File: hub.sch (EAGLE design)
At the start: 26 parts, among them U1 10118194-MICRO-USB, U2 LM3671MF-3.3/NOPBMF05A-M, U3 SN74LVC1T45DBVRDBV6-M, U4 SN74LVC1T45DBVRDBV6-M

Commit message: More component arrangement
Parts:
- JP7: value (none) -> GPIO
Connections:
- net GND: now also U1.GND$1, U1.GND$2, U1.GND$3, U1.GND$4, U1.GND$5; no longer U1.GND
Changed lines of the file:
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@@
 <part name="GND18" library="supply1" library_urn="urn:adsk.eagle:library:371" deviceset="GND" device=""/>
 <part name="U$2" library="nebrius" deviceset="ESP32-WROOM-32D" device=""/>
-<part name="JP7" library="pinhead" library_urn="urn:adsk.eagle:library:325" deviceset="PINHD-2X5" device="" package3d_urn="urn:adsk.eagle:package:22470/2"/>
+<part name="JP7" library="pinhead" library_urn="urn:adsk.eagle:library:325" deviceset="PINHD-2X5" device="" package3d_urn="urn:adsk.eagle:package:22470/2" value="GPIO"/>
 <part name="GND23" library="supply1" library_urn="urn:adsk.eagle:library:371" deviceset="GND" device=""/>
 <part name="P+10" library="supply1" library_urn="urn:adsk.eagle:library:371" deviceset="VCC" device=""/>
@@
 <part name="GND17" library="supply1" library_urn="urn:adsk.eagle:library:371" deviceset="GND" device=""/>
 <part name="P+9" library="supply1" library_urn="urn:adsk.eagle:library:371" deviceset="VCC" device=""/>
+<part name="GND20" library="supply1" library_urn="urn:adsk.eagle:library:371" deviceset="GND" device=""/>
 </parts>
 <sheets>
@@
 <attribute name="VALUE" x="139.7" y="0" size="1.778" layer="96"/>
 </instance>
+<instance part="GND20" gate="1" x="5.08" y="12.7" smashed="yes">
+<attribute name="VALUE" x="2.54" y="10.16" size="1.778" layer="96"/>
+</instance>
 </instances>
 <busses>
@@
 <net name="GND" class="0">
 <segment>
-<pinref part="U1" gate="G$1" pin="GND"/>
+<pinref part="U1" gate="G$1" pin="GND$1"/>
 <pinref part="GND1" gate="1" pin="GND"/>
 <wire x1="38.1" y1="17.78" x2="40.64" y2="17.78" width="0.1524" layer="91"/>
@@
 <wire x1="142.24" y1="5.08" x2="142.24" y2="7.62" width="0.1524" layer="91"/>
 </segment>
+<segment>
+<pinref part="U1" gate="G$1" pin="GND$2"/>
+<pinref part="GND20" gate="1" pin="GND"/>
+<wire x1="7.62" y1="25.4" x2="5.08" y2="25.4" width="0.1524" layer="91"/>
+<wire x1="5.08" y1="25.4" x2="5.08" y2="22.86" width="0.1524" layer="91"/>
+<pinref part="U1" gate="G$1" pin="GND$3"/>
+<wire x1="5.08" y1="22.86" x2="5.08" y2="20.32" width="0.1524" layer="91"/>
+<wire x1="5.08" y1="20.32" x2="5.08" y2="17.78" width="0.1524" layer="91"/>
+<wire x1="5.08" y1="17.78" x2="5.08" y2="15.24" width="0.1524" layer="91"/>
+<wire x1="7.62" y1="22.86" x2="5.08" y2="22.86" width="0.1524" layer="91"/>
+<junction x="5.08" y="22.86"/>
+<pinref part="U1" gate="G$1" pin="GND$4"/>
+<wire x1="7.62" y1="20.32" x2="5.08" y2="20.32" width="0.1524" layer="91"/>
+<junction x="5.08" y="20.32"/>
+<pinref part="U1" gate="G$1" pin="GND$5"/>
+<wire x1="7.62" y1="17.78" x2="5.08" y2="17.78" width="0.1524" layer="91"/>
+<junction x="5.08" y="17.78"/>
+</segment>
 </net>

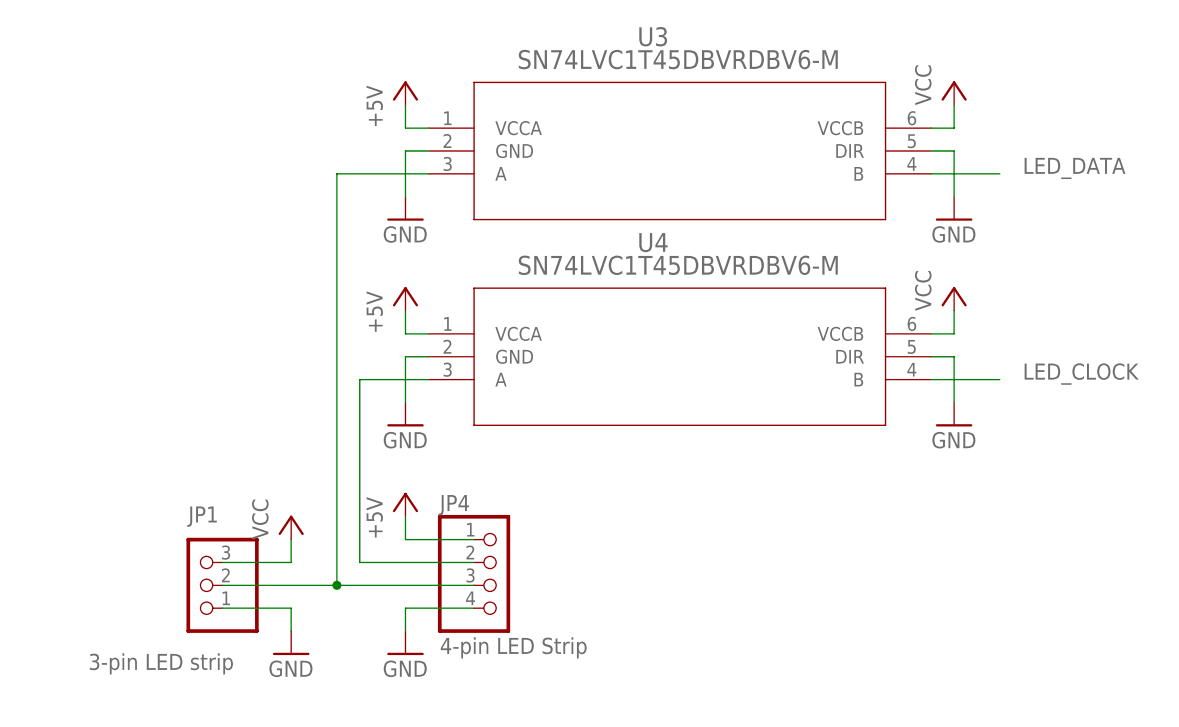
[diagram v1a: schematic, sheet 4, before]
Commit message: First draft of device placement
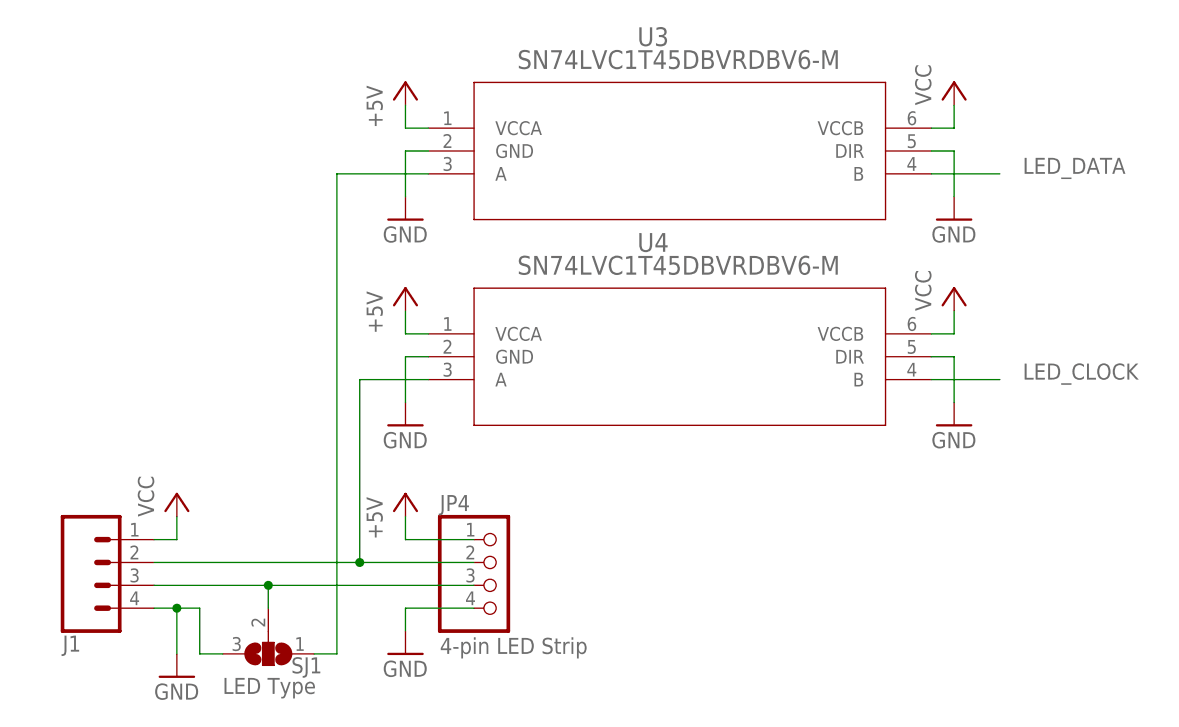
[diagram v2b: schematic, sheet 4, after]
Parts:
- removed JP1: 3-pin LED strip, pinhead:PINHD-1X3/90
- added J1: (no value), SparkFun-Connectors:CONN_04SCREW
- added SJ1: LED Type, jumper:SJ2W
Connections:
- new net N$7: J1.3, JP4.3, SJ1.2
- net GND: now also J1.4, SJ1.3; no longer JP1.1
- net N$8: now also SJ1.1; no longer JP1.2, JP4.3
- net N$9: now also J1.2
- net VCC: now also J1.1, JP2.3; no longer JP1.3
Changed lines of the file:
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@@
 <layer number="112" name="tSilk" color="7" fill="1" visible="no" active="yes"/>
 <layer number="113" name="IDFDebug" color="4" fill="1" visible="no" active="yes"/>
+<layer number="114" name="Badge_Outline" color="7" fill="1" visible="yes" active="yes"/>
+<layer number="115" name="ReferenceISLANDS" color="7" fill="1" visible="yes" active="yes"/>
 <layer number="116" name="Patch_BOT" color="9" fill="4" visible="no" active="yes"/>
 <layer number="118" name="Rect_Pads" color="7" fill="1" visible="no" active="yes"/>
@@
 <layer number="230" name="230bmp" color="7" fill="1" visible="no" active="yes"/>
 <layer number="231" name="231bmp" color="7" fill="1" visible="no" active="yes"/>
+<layer number="232" name="Eagle3D_PG2" color="7" fill="1" visible="yes" active="yes"/>
+<layer number="233" name="Eagle3D_PG3" color="7" fill="1" visible="yes" active="yes"/>
 <layer number="248" name="Housing" color="7" fill="1" visible="no" active="yes"/>
 <layer number="249" name="Edge" color="7" fill="1" visible="no" active="yes"/>
@@
 <part name="JP3" library="pinhead" library_urn="urn:adsk.eagle:library:325" deviceset="PINHD-2X3" device="" package3d_urn="urn:adsk.eagle:package:22462/2" value="JTAG"/>
 <part name="GND16" library="supply1" library_urn="urn:adsk.eagle:library:371" deviceset="GND" device=""/>
-<part name="JP1" library="pinhead" library_urn="urn:adsk.eagle:library:325" deviceset="PINHD-1X3" device="/90" package3d_urn="urn:adsk.eagle:package:22459/2" value="3-pin LED strip"/>
+<part name="GND20" library="supply1" library_urn="urn:adsk.eagle:library:371" deviceset="GND" device=""/>
+<part name="P+14" library="supply1" library_urn="urn:adsk.eagle:library:371" deviceset="VCC" device=""/>
+<part name="J1" library="SparkFun-Connectors" library_urn="urn:adsk.eagle:library:513" deviceset="CONN_04" device="SCREW" package3d_urn="urn:adsk.eagle:package:38090/1"/>
+<part name="P+9" library="supply1" library_urn="urn:adsk.eagle:library:371" deviceset="VCC" device=""/>
 <part name="GND17" library="supply1" library_urn="urn:adsk.eagle:library:371" deviceset="GND" device=""/>
-<part name="P+9" library="supply1" library_urn="urn:adsk.eagle:library:371" deviceset="VCC" device=""/>
-<part name="GND20" library="supply1" library_urn="urn:adsk.eagle:library:371" deviceset="GND" device=""/>
+<part name="SJ1" library="jumper" library_urn="urn:adsk.eagle:library:252" deviceset="SJ2W" device="" package3d_urn="urn:adsk.eagle:package:15474/1" value="LED Type"/>
 </parts>
 <sheets>
@@
 <attribute name="VALUE" x="25.4" y="43.18" size="1.778" layer="96" rot="R180"/>
 </instance>
+<instance part="P+14" gate="VCC" x="68.58" y="60.96" smashed="yes">
+<attribute name="VALUE" x="66.04" y="58.42" size="1.778" layer="96" rot="R90"/>
+</instance>
 </instances>
 <busses>
@@
 </segment>
 </net>
+<net name="VCC" class="0">
+<segment>
+<pinref part="JP2" gate="A" pin="3"/>
+<pinref part="P+14" gate="VCC" pin="VCC"/>
+<wire x1="78.74" y1="50.8" x2="68.58" y2="50.8" width="0.1524" layer="91"/>
+<wire x1="68.58" y1="50.8" x2="68.58" y2="58.42" width="0.1524" layer="91"/>
+</segment>
+</net>
 </nets>
 </sheet>
@@
 <attribute name="VALUE" x="19.05" y="43.18" size="1.778" layer="96"/>
 </instance>
-<instance part="JP1" gate="A" x="-7.62" y="50.8" smashed="yes" rot="R180">
-<attribute name="NAME" x="-8.89" y="57.785" size="1.778" layer="95" rot="R180" align="top-right"/>
-<attribute name="VALUE" x="-3.81" y="43.18" size="1.778" layer="96" rot="R180"/>
-</instance>
-<instance part="GND17" gate="1" x="2.54" y="43.18" smashed="yes">
-<attribute name="VALUE" x="0" y="40.64" size="1.778" layer="96"/>
-</instance>
-<instance part="P+9" gate="VCC" x="2.54" y="58.42" smashed="yes">
-<attribute name="VALUE" x="0" y="55.88" size="1.778" layer="96" rot="R90"/>
+<instance part="J1" gate="G$1" x="-17.78" y="53.34" smashed="yes" rot="MR180">
+<attribute name="VALUE" x="-22.86" y="60.706" size="1.778" layer="96" font="vector" rot="MR180"/>
+<attribute name="NAME" x="-22.86" y="45.212" size="1.778" layer="95" font="vector" rot="MR180"/>
+</instance>
+<instance part="P+9" gate="VCC" x="-10.16" y="60.96" smashed="yes">
+<attribute name="VALUE" x="-12.7" y="58.42" size="1.778" layer="96" rot="R90"/>
+</instance>
+<instance part="GND17" gate="1" x="-10.16" y="40.64" smashed="yes">
+<attribute name="VALUE" x="-12.7" y="38.1" size="1.778" layer="96"/>
+</instance>
+<instance part="SJ1" gate="G$1" x="0" y="43.18" smashed="yes" rot="R270">
+<attribute name="NAME" x="2.54" y="41.021" size="1.778" layer="95"/>
+<attribute name="VALUE" x="-5.08" y="38.735" size="1.778" layer="96"/>
 </instance>
 </instances>
@@
 </segment>
 <segment>
-<pinref part="JP1" gate="A" pin="1"/>
 <pinref part="GND17" gate="1" pin="GND"/>
-<wire x1="-5.08" y1="48.26" x2="2.54" y2="48.26" width="0.1524" layer="91"/>
-<wire x1="2.54" y1="48.26" x2="2.54" y2="45.72" width="0.1524" layer="91"/>
+<wire x1="-10.16" y1="48.26" x2="-10.16" y2="43.18" width="0.1524" layer="91"/>
+<pinref part="J1" gate="G$1" pin="4"/>
+<wire x1="-12.7" y1="48.26" x2="-10.16" y2="48.26" width="0.1524" layer="91"/>
+<wire x1="-5.08" y1="43.18" x2="-7.62" y2="43.18" width="0.1524" layer="91"/>
+<wire x1="-7.62" y1="43.18" x2="-7.62" y2="48.26" width="0.1524" layer="91"/>
+<wire x1="-7.62" y1="48.26" x2="-10.16" y2="48.26" width="0.1524" layer="91"/>
+<junction x="-10.16" y="48.26"/>
+<pinref part="SJ1" gate="G$1" pin="3"/>
 </segment>
 </net>
@@
 </segment>
 <segment>
-<pinref part="JP1" gate="A" pin="3"/>
-<wire x1="-5.08" y1="53.34" x2="2.54" y2="53.34" width="0.1524" layer="91"/>
 <pinref part="P+9" gate="VCC" pin="VCC"/>
-<wire x1="2.54" y1="53.34" x2="2.54" y2="55.88" width="0.1524" layer="91"/>
+<wire x1="-10.16" y1="55.88" x2="-10.16" y2="58.42" width="0.1524" layer="91"/>
+<pinref part="J1" gate="G$1" pin="1"/>
+<wire x1="-12.7" y1="55.88" x2="-10.16" y2="55.88" width="0.1524" layer="91"/>
 </segment>
 </net>
@@
 <segment>
 <pinref part="U3" gate="A" pin="A"/>
-<wire x1="7.62" y1="50.8" x2="7.62" y2="96.52" width="0.1524" layer="91"/>
 <wire x1="7.62" y1="96.52" x2="17.78" y2="96.52" width="0.1524" layer="91"/>
-<pinref part="JP1" gate="A" pin="2"/>
-<wire x1="-5.08" y1="50.8" x2="7.62" y2="50.8" width="0.1524" layer="91"/>
-<pinref part="JP4" gate="A" pin="3"/>
-<wire x1="22.86" y1="50.8" x2="7.62" y2="50.8" width="0.1524" layer="91"/>
-<junction x="7.62" y="50.8"/>
+<wire x1="7.62" y1="96.52" x2="7.62" y2="43.18" width="0.1524" layer="91"/>
+<wire x1="7.62" y1="43.18" x2="5.08" y2="43.18" width="0.1524" layer="91"/>
+<pinref part="SJ1" gate="G$1" pin="1"/>
 </segment>
 </net>
@@
 <wire x1="22.86" y1="53.34" x2="10.16" y2="53.34" width="0.1524" layer="91"/>
 <wire x1="10.16" y1="53.34" x2="10.16" y2="73.66" width="0.1524" layer="91"/>
+<pinref part="J1" gate="G$1" pin="2"/>
+<wire x1="-12.7" y1="53.34" x2="10.16" y2="53.34" width="0.1524" layer="91"/>
+<junction x="10.16" y="53.34"/>
 </segment>
 </net>
@@
 </segment>
 </net>
+<net name="N$7" class="0">
+<segment>
+<wire x1="0" y1="48.26" x2="0" y2="50.8" width="0.1524" layer="91"/>
+<pinref part="JP4" gate="A" pin="3"/>
+<wire x1="0" y1="50.8" x2="22.86" y2="50.8" width="0.1524" layer="91"/>
+<pinref part="J1" gate="G$1" pin="3"/>
+<wire x1="-12.7" y1="50.8" x2="0" y2="50.8" width="0.1524" layer="91"/>
+<junction x="0" y="50.8"/>
+<pinref part="SJ1" gate="G$1" pin="2"/>
+</segment>
+</net>

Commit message: First draft of component layout
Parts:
- removed JP4: 4-pin LED Strip, pinhead:PINHD-1X4/90
- added JP1: (no value), pinhead:PINHD-1X4
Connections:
- net +5V: now also J1.1, JP1.1; no longer JP4.1
- net GND: now also JP1.4; no longer JP4.4
- net N$7: now also JP1.3; no longer JP4.3
- net N$9: now also JP1.2; no longer JP4.2
- net VCC: no longer J1.1
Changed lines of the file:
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@@
 <part name="R4" library="rcl" library_urn="urn:adsk.eagle:library:334" deviceset="R-US_" device="R0805" package3d_urn="urn:adsk.eagle:package:23553/2" value="10k"/>
 <part name="P+12" library="supply1" library_urn="urn:adsk.eagle:library:371" deviceset="VCC" device=""/>
-<part name="JP4" library="pinhead" library_urn="urn:adsk.eagle:library:325" deviceset="PINHD-1X4" device="/90" package3d_urn="urn:adsk.eagle:package:22404/2" value="4-pin LED Strip"/>
 <part name="R6" library="rcl" library_urn="urn:adsk.eagle:library:334" deviceset="R-US_" device="R0805" package3d_urn="urn:adsk.eagle:package:23553/2" value="220"/>
 <part name="LED1" library="led" library_urn="urn:adsk.eagle:library:259" deviceset="LED" device="CHIPLED_0805" package3d_urn="urn:adsk.eagle:package:15821/2" value="Power"/>
@@
 <part name="P+14" library="supply1" library_urn="urn:adsk.eagle:library:371" deviceset="VCC" device=""/>
 <part name="J1" library="SparkFun-Connectors" library_urn="urn:adsk.eagle:library:513" deviceset="CONN_04" device="SCREW" package3d_urn="urn:adsk.eagle:package:38090/1"/>
-<part name="P+9" library="supply1" library_urn="urn:adsk.eagle:library:371" deviceset="VCC" device=""/>
 <part name="GND17" library="supply1" library_urn="urn:adsk.eagle:library:371" deviceset="GND" device=""/>
 <part name="SJ1" library="jumper" library_urn="urn:adsk.eagle:library:252" deviceset="SJ2W" device="" package3d_urn="urn:adsk.eagle:package:15474/1" value="LED Type"/>
+<part name="JP1" library="pinhead" library_urn="urn:adsk.eagle:library:325" deviceset="PINHD-1X4" device="" package3d_urn="urn:adsk.eagle:package:22407/2"/>
+<part name="P+9" library="supply1" library_urn="urn:adsk.eagle:library:371" deviceset="+5V" device=""/>
 </parts>
 <sheets>
@@
 <attribute name="VALUE" x="12.7" y="55.88" size="1.778" layer="96" rot="R90"/>
 </instance>
-<instance part="JP4" gate="A" x="25.4" y="50.8" smashed="yes">
-<attribute name="NAME" x="19.05" y="59.055" size="1.778" layer="95"/>
-<attribute name="VALUE" x="19.05" y="43.18" size="1.778" layer="96"/>
-</instance>
 <instance part="J1" gate="G$1" x="-17.78" y="53.34" smashed="yes" rot="MR180">
 <attribute name="VALUE" x="-22.86" y="60.706" size="1.778" layer="96" font="vector" rot="MR180"/>
 <attribute name="NAME" x="-22.86" y="45.212" size="1.778" layer="95" font="vector" rot="MR180"/>
 </instance>
-<instance part="P+9" gate="VCC" x="-10.16" y="60.96" smashed="yes">
-<attribute name="VALUE" x="-12.7" y="58.42" size="1.778" layer="96" rot="R90"/>
-</instance>
 <instance part="GND17" gate="1" x="-10.16" y="40.64" smashed="yes">
 <attribute name="VALUE" x="-12.7" y="38.1" size="1.778" layer="96"/>
@@
 <attribute name="NAME" x="2.54" y="41.021" size="1.778" layer="95"/>
 <attribute name="VALUE" x="-5.08" y="38.735" size="1.778" layer="96"/>
+</instance>
+<instance part="JP1" gate="A" x="25.4" y="50.8" smashed="yes">
+<attribute name="NAME" x="19.05" y="59.055" size="1.778" layer="95"/>
+<attribute name="VALUE" x="19.05" y="43.18" size="1.778" layer="96"/>
+</instance>
+<instance part="P+9" gate="1" x="-10.16" y="60.96" smashed="yes">
+<attribute name="VALUE" x="-5.08" y="55.88" size="1.778" layer="96" rot="R90"/>
 </instance>
 </instances>
@@
 <wire x1="22.86" y1="48.26" x2="15.24" y2="48.26" width="0.1524" layer="91"/>
 <wire x1="15.24" y1="48.26" x2="15.24" y2="45.72" width="0.1524" layer="91"/>
-<pinref part="JP4" gate="A" pin="4"/>
+<pinref part="JP1" gate="A" pin="4"/>
 </segment>
 <segment>
@@
 <wire x1="76.2" y1="78.74" x2="76.2" y2="81.28" width="0.1524" layer="91"/>
 </segment>
-<segment>
-<pinref part="P+9" gate="VCC" pin="VCC"/>
-<wire x1="-10.16" y1="55.88" x2="-10.16" y2="58.42" width="0.1524" layer="91"/>
-<pinref part="J1" gate="G$1" pin="1"/>
-<wire x1="-12.7" y1="55.88" x2="-10.16" y2="55.88" width="0.1524" layer="91"/>
-</segment>
 </net>
 <net name="N$8" class="0">
@@
 <pinref part="U4" gate="A" pin="A"/>
 <wire x1="10.16" y1="73.66" x2="17.78" y2="73.66" width="0.1524" layer="91"/>
-<pinref part="JP4" gate="A" pin="2"/>
 <wire x1="22.86" y1="53.34" x2="10.16" y2="53.34" width="0.1524" layer="91"/>
 <wire x1="10.16" y1="53.34" x2="10.16" y2="73.66" width="0.1524" layer="91"/>
@@
 <wire x1="-12.7" y1="53.34" x2="10.16" y2="53.34" width="0.1524" layer="91"/>
 <junction x="10.16" y="53.34"/>
+<pinref part="JP1" gate="A" pin="2"/>
 </segment>
 </net>
@@
 <wire x1="15.24" y1="55.88" x2="15.24" y2="58.42" width="0.1524" layer="91"/>
 <pinref part="P+2" gate="1" pin="+5V"/>
-<pinref part="JP4" gate="A" pin="1"/>
+<pinref part="JP1" gate="A" pin="1"/>
+</segment>
+<segment>
+<wire x1="-10.16" y1="55.88" x2="-10.16" y2="58.42" width="0.1524" layer="91"/>
+<pinref part="J1" gate="G$1" pin="1"/>
+<wire x1="-12.7" y1="55.88" x2="-10.16" y2="55.88" width="0.1524" layer="91"/>
+<pinref part="P+9" gate="1" pin="+5V"/>
 </segment>
 </net>
@@
 <segment>
 <wire x1="0" y1="48.26" x2="0" y2="50.8" width="0.1524" layer="91"/>
-<pinref part="JP4" gate="A" pin="3"/>
 <wire x1="0" y1="50.8" x2="22.86" y2="50.8" width="0.1524" layer="91"/>
 <pinref part="J1" gate="G$1" pin="3"/>
@@
 <junction x="0" y="50.8"/>
 <pinref part="SJ1" gate="G$1" pin="2"/>
-</segment>
-</net>
+<pinref part="JP1" gate="A" pin="3"/>
+</segment>
+</net>

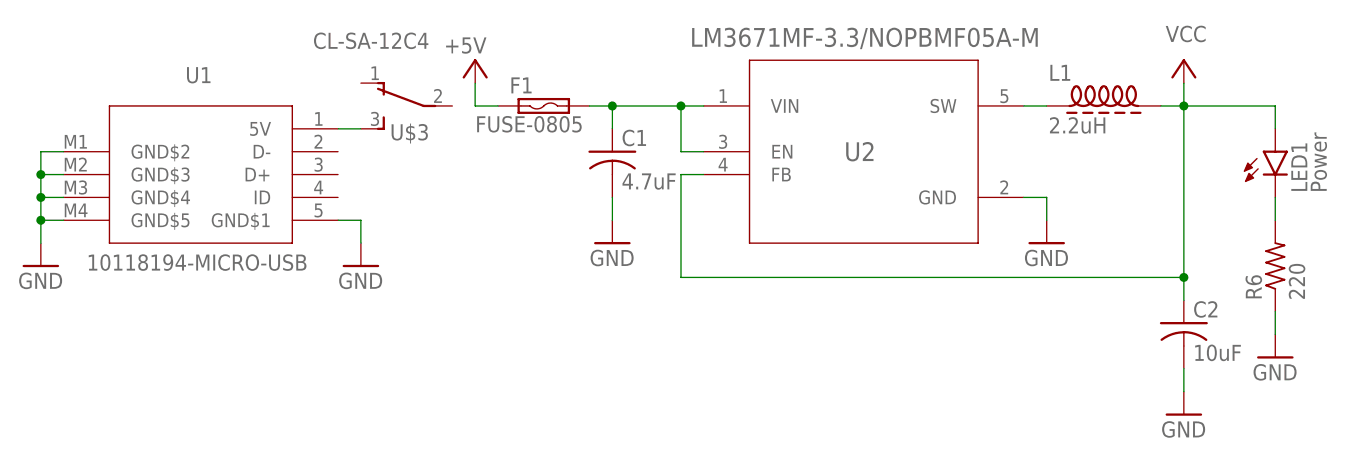
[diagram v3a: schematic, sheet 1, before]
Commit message: Finished placing components and started laying out traces
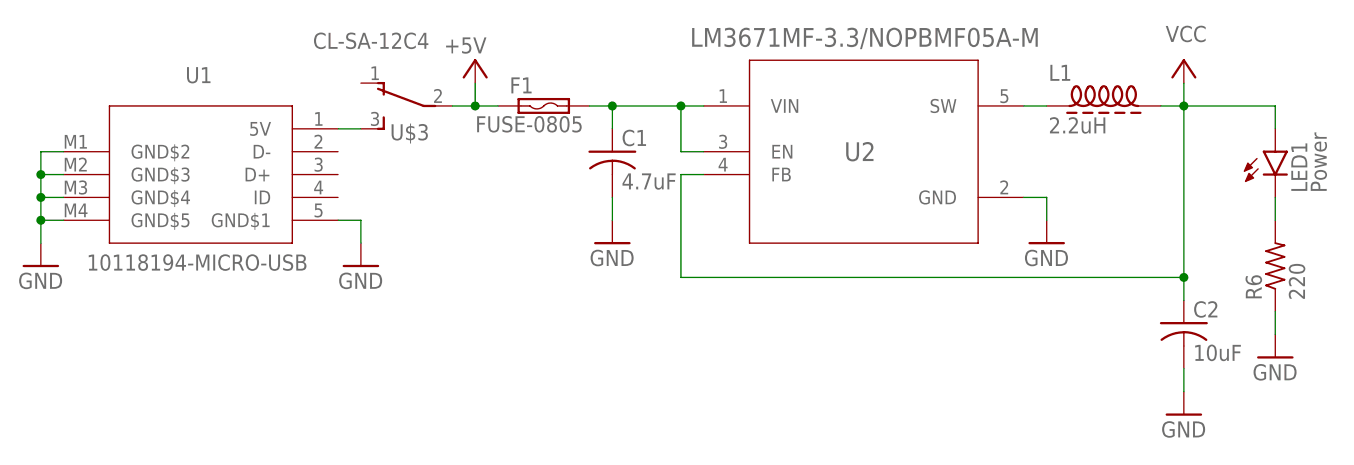
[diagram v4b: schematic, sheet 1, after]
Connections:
- net +5V: now also U$3.2
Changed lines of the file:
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@@
 <pinref part="F1" gate="A" pin="1"/>
 <pinref part="P+1" gate="1" pin="+5V"/>
+<pinref part="U$3" gate="A" pin="2"/>
+<wire x1="50.8" y1="30.48" x2="53.34" y2="30.48" width="0.1524" layer="91"/>
+<junction x="53.34" y="30.48"/>
 </segment>
 </net>
